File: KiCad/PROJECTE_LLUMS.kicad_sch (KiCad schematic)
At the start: 9 parts, among them Q1 IRLZ44N, U1 LM2596S-5, U2 LM1117MP-3.3, U3 MCP2551-I-SN

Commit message: part llums
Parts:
- added D2, D3, D4, D5, D6: LED, LED_THT:LED_D5.0mm, symbol Device:LED
- added D7: 1N5408, Diode_THT:D_DO-201AD_P15.24mm_Horizontal, symbol Diode:1N5408
- added J1: CONNECTOR_MOTOR, Connector_JST:JST_VH_B2P-VH_1x02_P3.96mm_Vertical, symbol Connector:Conn_01x02_Pin
- added Q2, Q3, Q4, Q5, Q6, Q7: IRLZ44N, Package_TO_SOT_THT:TO-220-3_Vertical, symbol Transistor_FET:IRLZ44N
- added R2, R3, R4, R5, R6: 1k, Relay_SMD:Relay_2P2T_10x6mm_TE_IMxxG, symbol Device:R
- R1: footprint (none) -> Relay_SMD:Relay_2P2T_10x6mm_TE_IMxxG
- renumbered C_in to C_in1, C_out to C_out2
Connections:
- net GND: now also Q2.3 (S), Q3.3 (S), Q4.3 (S), Q5.3 (S), Q6.3 (S), Q7.3 (S)
- new net: D7.1 (K), D7.2 (A), J1.2 (Pin_2), Q7.2 (D)
- new net: Q6.2 (D), R6.1
- new net: D2.1 (K), R2.2
- new net: Q4.2 (D), R5.1
- new net: D5.1 (K), R5.2
- new net: Q5.2 (D), R4.1
- new net: D4.1 (K), R4.2
- new net: Q2.2 (D), R3.1
- new net: D3.1 (K), R3.2
- new net: D6.1 (K), R6.2
- new net: Q3.2 (D), R2.1
- new net +12V: D2.2 (A), D3.2 (A), D4.2 (A), D5.2 (A), D6.2 (A), J1.1 (Pin_1)
- new net PWM: Q2.1 (G), Q3.1 (G), Q4.1 (G), Q5.1 (G), Q6.1 (G), Q7.1 (G)
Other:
- moved on the sheet: C_out1, Q1, R1, U3

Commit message: llums bé pagina nova
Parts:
- removed C_in1, C_out2: 100uF, symbol Device:C
- removed C_out1: 100nF, symbol Device:C
- removed D1: 1N4148WT, Diode_SMD:D_SOD-523, symbol Diode:1N4148WT
- removed D2, D3, D4, D5, D6: LED, LED_THT:LED_D5.0mm, symbol Device:LED
- removed D7: 1N5408, Diode_THT:D_DO-201AD_P15.24mm_Horizontal, symbol Diode:1N5408
- removed J1: CONNECTOR_MOTOR, Connector_JST:JST_VH_B2P-VH_1x02_P3.96mm_Vertical, symbol Connector:Conn_01x02_Pin
- removed Q1, Q2, Q3, Q4, Q5, Q6, Q7: IRLZ44N, Package_TO_SOT_THT:TO-220-3_Vertical, symbol Transistor_FET:IRLZ44N
- removed R1: 12O, Relay_SMD:Relay_2P2T_10x6mm_TE_IMxxG, symbol Device:R
- removed R2, R3, R4, R5, R6: 1k, Relay_SMD:Relay_2P2T_10x6mm_TE_IMxxG, symbol Device:R
- removed U1: LM2596S-5, Package_TO_SOT_SMD:TO-263-5_TabPin3, symbol Regulator_Switching:LM2596S-5
- removed U2: LM1117MP-3.3, Package_TO_SOT_SMD:SOT-223-3_TabPin2, symbol Regulator_Linear:LM1117MP-3.3
- removed U3: MCP2551-I-SN, Package_SO:SOIC-8_3.9x4.9mm_P1.27mm, symbol Interface_CAN_LIN:MCP2551-I-SN
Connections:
- no-connect marks 1 -> 0
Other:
- added sheet llums (untitled.kicad_sch)

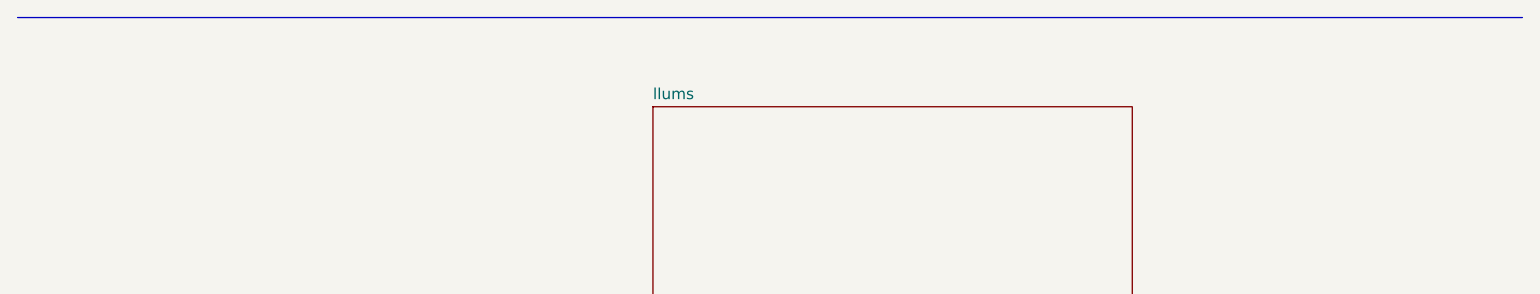
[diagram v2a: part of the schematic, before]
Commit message: llums bé amb les etiquetes bé
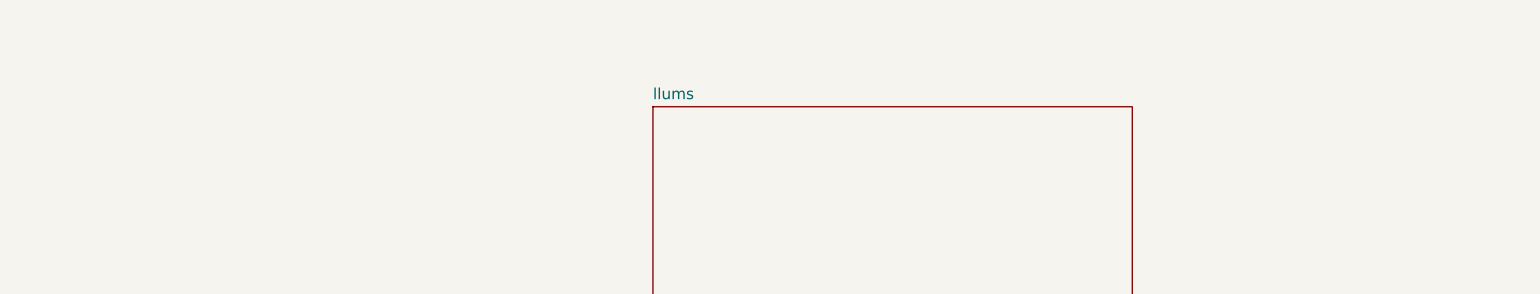
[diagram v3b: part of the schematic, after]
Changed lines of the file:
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@@
 	(generator_version "9.0")
 	(paper "A4")
-	(polyline
-		(pts
-			(xy 110.49 93.98) (xy 281.94 93.98)
-		)
-		(stroke
-			(width 0)
-			(type default)
-		)
-	)
 	(sheet
 		(at 182.88 104.14)

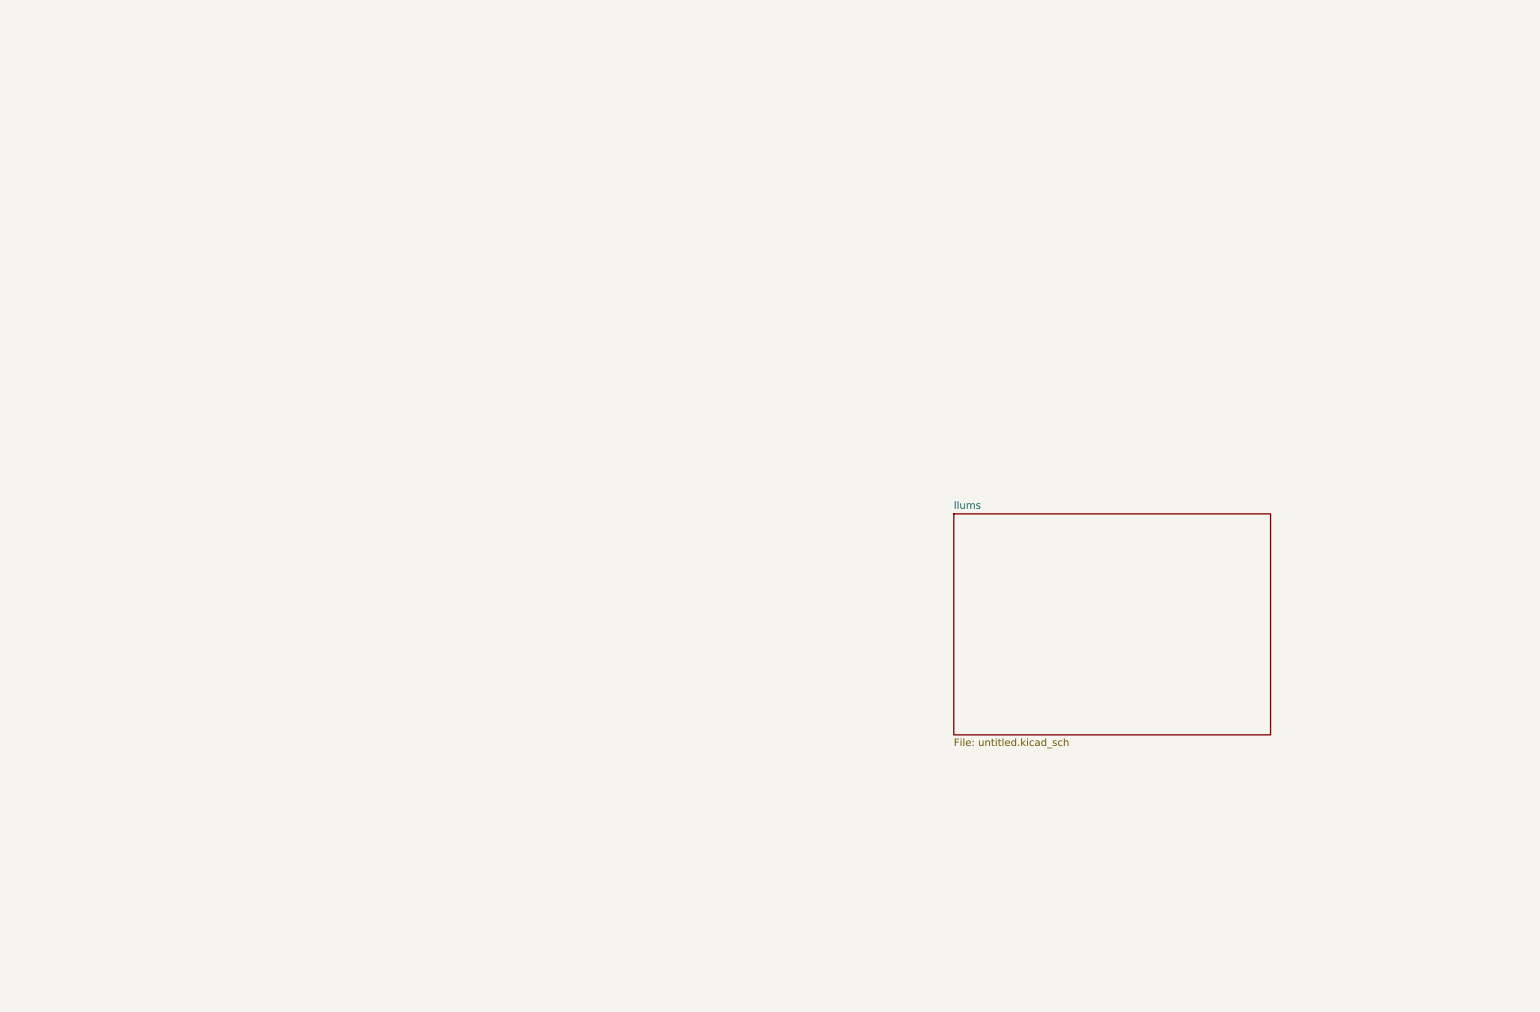
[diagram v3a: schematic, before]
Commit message: esquemàtic amb totes les cel·les
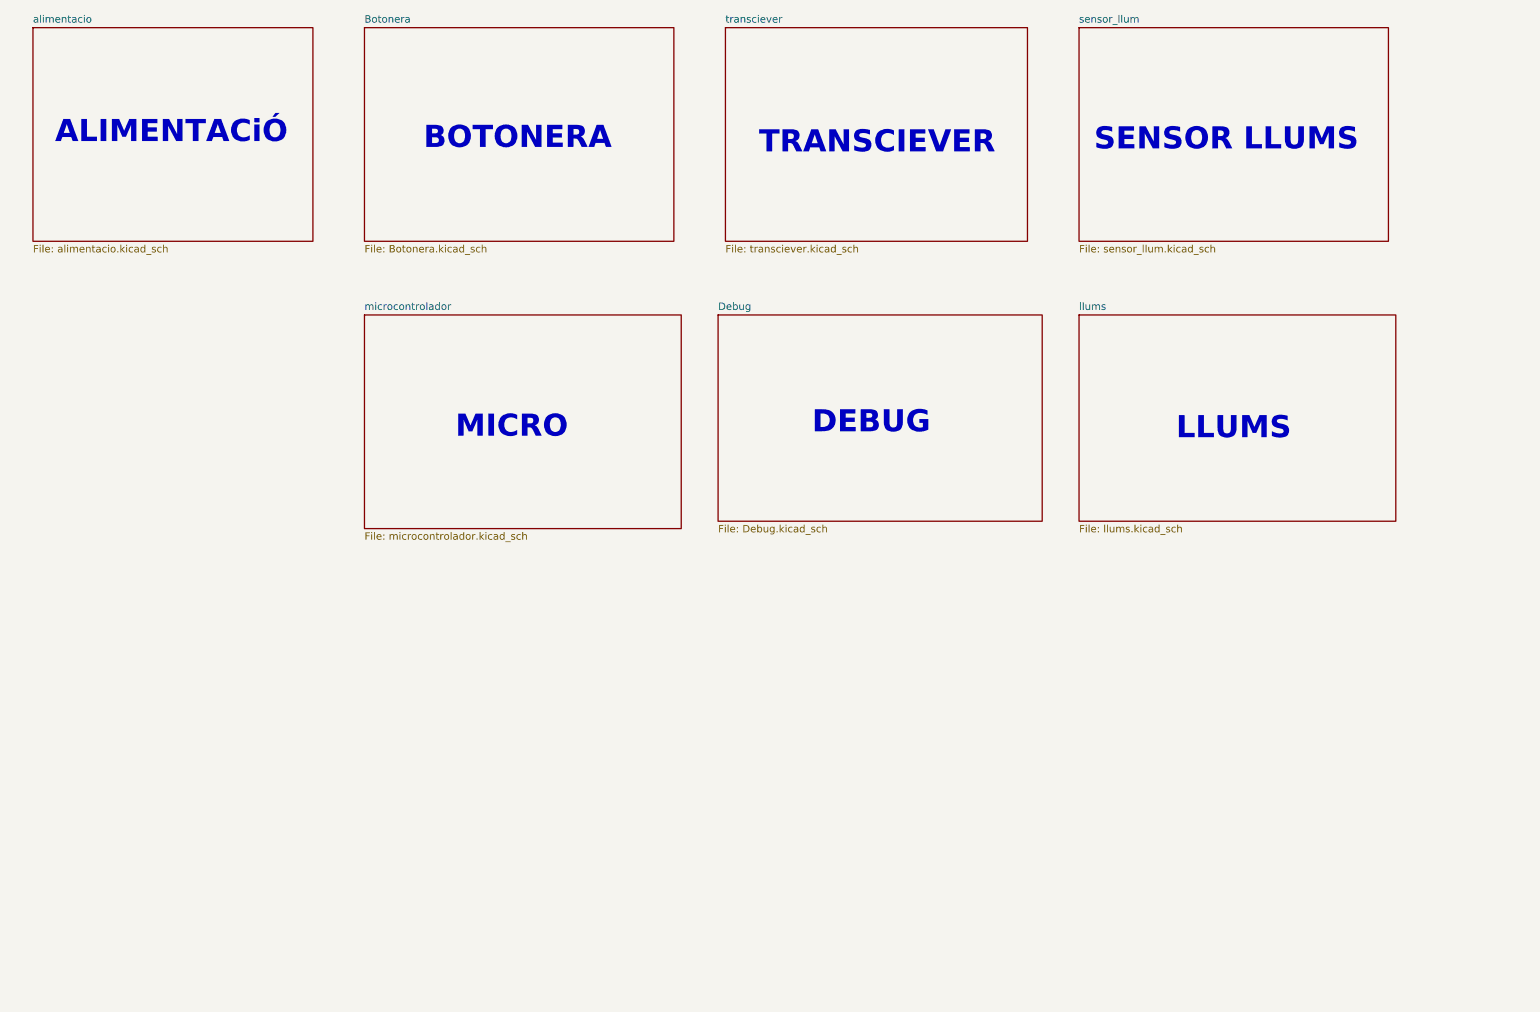
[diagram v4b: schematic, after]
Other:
- added sheet Botonera (Botonera.kicad_sch)
- added sheet Debug (Debug.kicad_sch)
- added sheet alimentacio (alimentacio.kicad_sch)
- added sheet microcontrolador (microcontrolador.kicad_sch)
- added sheet sensor_llum (sensor_llum.kicad_sch)
- added sheet transciever (transciever.kicad_sch)
- sheet llums: file untitled.kicad_sch -> llums.kicad_sch
- note added: "ALIMENTACiÓ"
- note added: "BOTONERA"
- note added: "DEBUG"
- note added: "LLUMS"
- note added: "MICRO"
- note added: "SENSOR LLUMS"
- note added: "TRANSCIEVER"

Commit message: ERC i footprints
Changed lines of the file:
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@@
 	(text "DEBUG\n"
 		(exclude_from_sim no)
-		(at 168.656 88.392 0)
+		(at 175.006 94.742 0)
 		(effects
 			(font
@@
 	(text "ALIMENTACiÓ"
 		(exclude_from_sim no)
-		(at 48.006 38.354 0)
+		(at 54.356 44.704 0)
 		(effects
 			(font
@@
 	(text "MICRO"
 		(exclude_from_sim no)
-		(at 106.68 89.154 0)
+		(at 113.03 95.504 0)
 		(effects
 			(font
@@
 	(text "LLUMS\n"
 		(exclude_from_sim no)
-		(at 231.14 89.408 0)
+		(at 237.49 95.758 0)
 		(effects
 			(font
@@
 	(text "TRANSCIEVER\n"
 		(exclude_from_sim no)
-		(at 169.672 40.132 0)
+		(at 176.022 46.482 0)
 		(effects
 			(font
@@
 	(text "BOTONERA\n"
 		(exclude_from_sim no)
-		(at 107.696 39.37 0)
+		(at 114.046 45.72 0)
 		(effects
 			(font
@@
 	(text "SENSOR LLUMS\n"
 		(exclude_from_sim no)
-		(at 229.87 39.624 0)
-		(effects
-			(font
-				(size 3.81 3.81)
-				(thickness 0.762)
-				(bold yes)
-			)
-		)
-	)
-	(sheet
-		(at 204.47 69.85)
+		(at 236.22 45.974 0)
+		(effects
+			(font
+				(size 3.81 3.81)
+				(thickness 0.762)
+				(bold yes)
+			)
+		)
+	)
+	(sheet
+		(at 210.82 76.2)
 		(size 54.61 35.56)
 		(exclude_from_sim no)
@@
 		)
 		(property "Sheetname" "llums"
-			(at 204.47 69.1384 0)
+			(at 210.82 75.4884 0)
 			(effects
 				(font
@@
 		)
 		(property "Sheetfile" "llums.kicad_sch"
-			(at 204.47 105.9946 0)
+			(at 210.82 112.3446 0)
 			(effects
 				(font
@@
 	)
 	(sheet
-		(at 204.47 20.32)
+		(at 210.82 26.67)
 		(size 53.34 36.83)
 		(exclude_from_sim no)
@@
 		)
 		(property "Sheetname" "sensor_llum"
-			(at 204.47 19.6084 0)
+			(at 210.82 25.9584 0)
 			(effects
 				(font
@@
 		)
 		(property "Sheetfile" "sensor_llum.kicad_sch"
-			(at 204.47 57.7346 0)
+			(at 210.82 64.0846 0)
 			(effects
 				(font
@@
 	)
 	(sheet
-		(at 81.28 69.85)
+		(at 87.63 76.2)
 		(size 54.61 36.83)
 		(exclude_from_sim no)
@@
 		)
 		(property "Sheetname" "microcontrolador"
-			(at 81.28 69.1384 0)
+			(at 87.63 75.4884 0)
 			(effects
 				(font
@@
 		)
 		(property "Sheetfile" "microcontrolador.kicad_sch"
-			(at 81.28 107.2646 0)
+			(at 87.63 113.6146 0)
 			(effects
 				(font
@@
 	)
 	(sheet
-		(at 81.28 20.32)
+		(at 87.63 26.67)
 		(size 53.34 36.83)
 		(exclude_from_sim no)
@@
 		)
 		(property "Sheetname" "Botonera"
-			(at 81.28 19.6084 0)
+			(at 87.63 25.9584 0)
 			(effects
 				(font
@@
 		)
 		(property "Sheetfile" "Botonera.kicad_sch"
-			(at 81.28 57.7346 0)
+			(at 87.63 64.0846 0)
 			(effects
 				(font
@@
 	)
 	(sheet
-		(at 24.13 20.32)
+		(at 30.48 26.67)
 		(size 48.26 36.83)
 		(exclude_from_sim no)
@@
 		)
 		(property "Sheetname" "alimentacio"
-			(at 24.13 19.6084 0)
+			(at 30.48 25.9584 0)
 			(effects
 				(font
@@
 		)
 		(property "Sheetfile" "alimentacio.kicad_sch"
-			(at 24.13 57.7346 0)
+			(at 30.48 64.0846 0)
 			(effects
 				(font
@@
 	)
 	(sheet
-		(at 142.24 69.85)
+		(at 148.59 76.2)
 		(size 55.88 35.56)
 		(exclude_from_sim no)
@@
 		)
 		(property "Sheetname" "Debug"
-			(at 142.24 69.1384 0)
+			(at 148.59 75.4884 0)
 			(effects
 				(font
@@
 		)
 		(property "Sheetfile" "Debug.kicad_sch"
-			(at 142.24 105.9946 0)
+			(at 148.59 112.3446 0)
 			(effects
 				(font
@@
 	)
 	(sheet
-		(at 143.51 20.32)
+		(at 149.86 26.67)
 		(size 52.07 36.83)
 		(exclude_from_sim no)
@@
 		)
 		(property "Sheetname" "transciever"
-			(at 143.51 19.6084 0)
+			(at 149.86 25.9584 0)
 			(effects
 				(font
@@
 		)
 		(property "Sheetfile" "transciever.kicad_sch"
-			(at 143.51 57.7346 0)
-			(effects
-				(font
+			(at 149.86 64.0846 0)
+			(effects
+				(font

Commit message: correcció d'errors CADLAB, falten els de llums i un parell que no entenc
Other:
- removed sheet Debug
- note removed: "DEBUG"
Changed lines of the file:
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@@
 	(generator_version "9.0")
 	(paper "A4")
-	(text "DEBUG\n"
-		(exclude_from_sim no)
-		(at 175.006 94.742 0)
-		(effects
-			(font
-				(size 3.81 3.81)
-				(thickness 0.762)
-				(bold yes)
-			)
-		)
-	)
 	(text "ALIMENTACiÓ"
 		(exclude_from_sim no)
@@
 				)
 			)
-		)
-	)
-	(sheet
-		(at 148.59 76.2)
-		(size 55.88 35.56)
-		(exclude_from_sim no)
-		(in_bom yes)
-		(on_board yes)
-		(dnp no)
-		(fields_autoplaced yes)
-		(stroke
-			(width 0.1524)
-			(type solid)
-		)
-		(fill
-			(color 0 0 0 0.0000)
-		)
-		(property "Sheetname" "Debug"
-			(at 148.59 75.4884 0)
-			(effects
-				(font
-					(size 1.27 1.27)
-				)
-				(justify left bottom)
-			)
-		)
-		(property "Sheetfile" "Debug.kicad_sch"
-			(at 148.59 112.3446 0)
-			(effects
-				(font
-					(size 1.27 1.27)
-				)
-				(justify left top)
-			)
-		)
-		(instances
-			(project "PROJECTE_LLUMS"
-				(path "/b4874c87-978f-427f-bc45-3635f8629977"
-					(page "8")
-				)
-			)
